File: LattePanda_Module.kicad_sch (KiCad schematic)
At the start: 3 parts

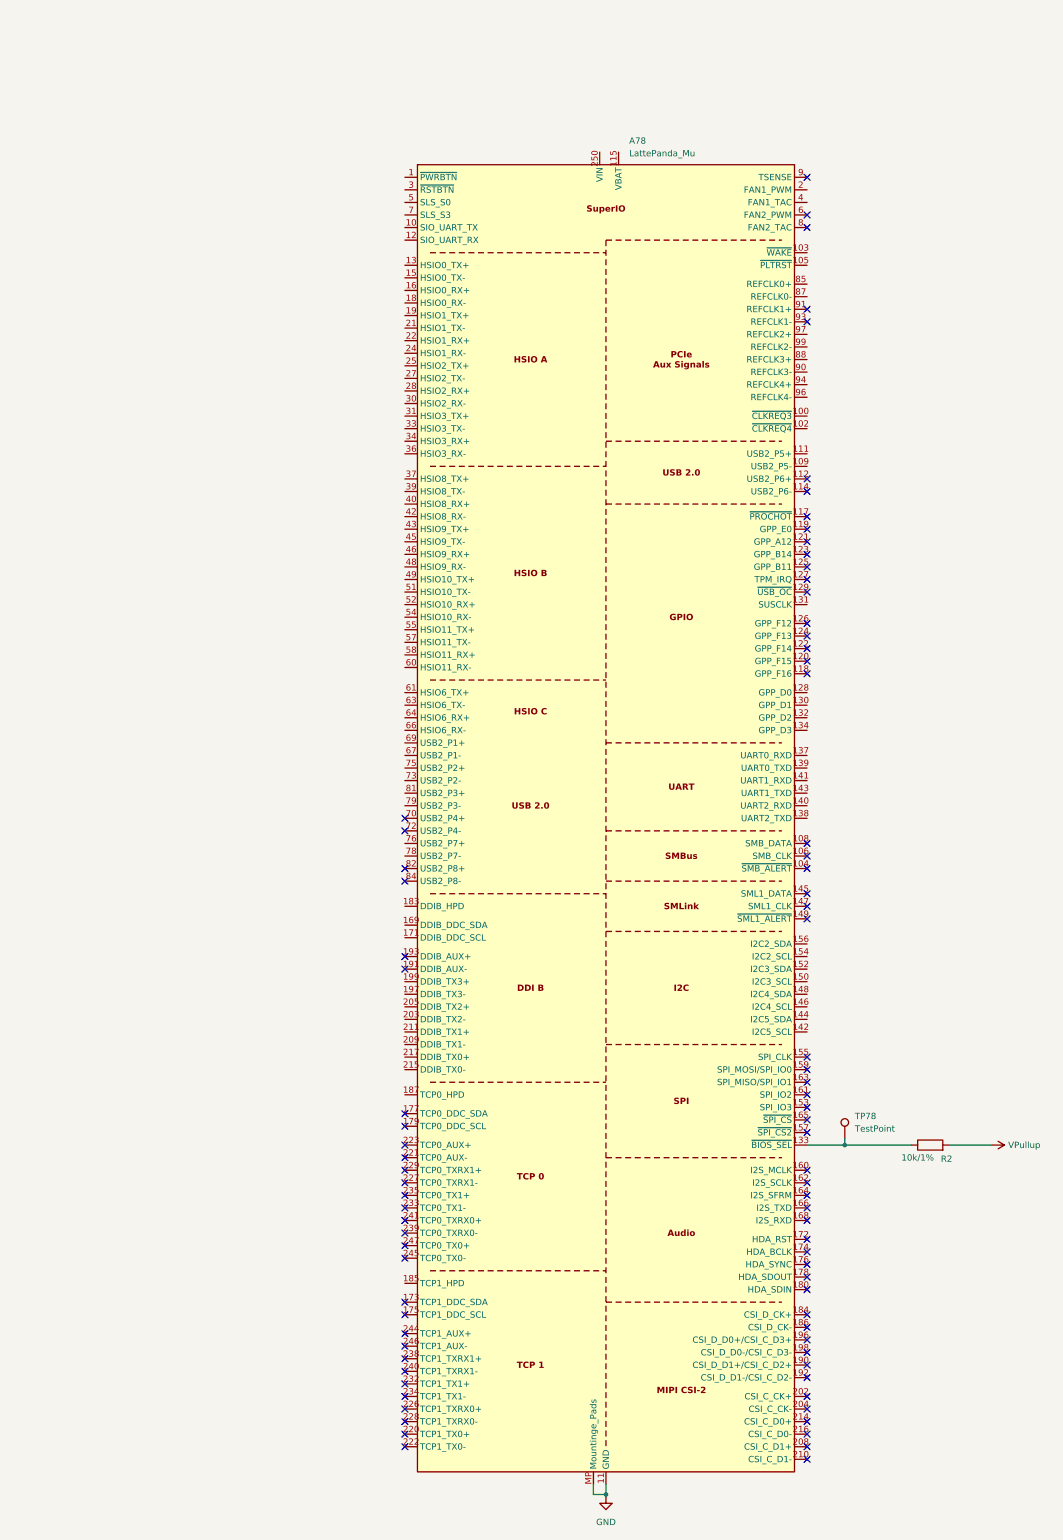
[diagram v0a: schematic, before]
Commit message: Added module pin symnbols and pull down resistors
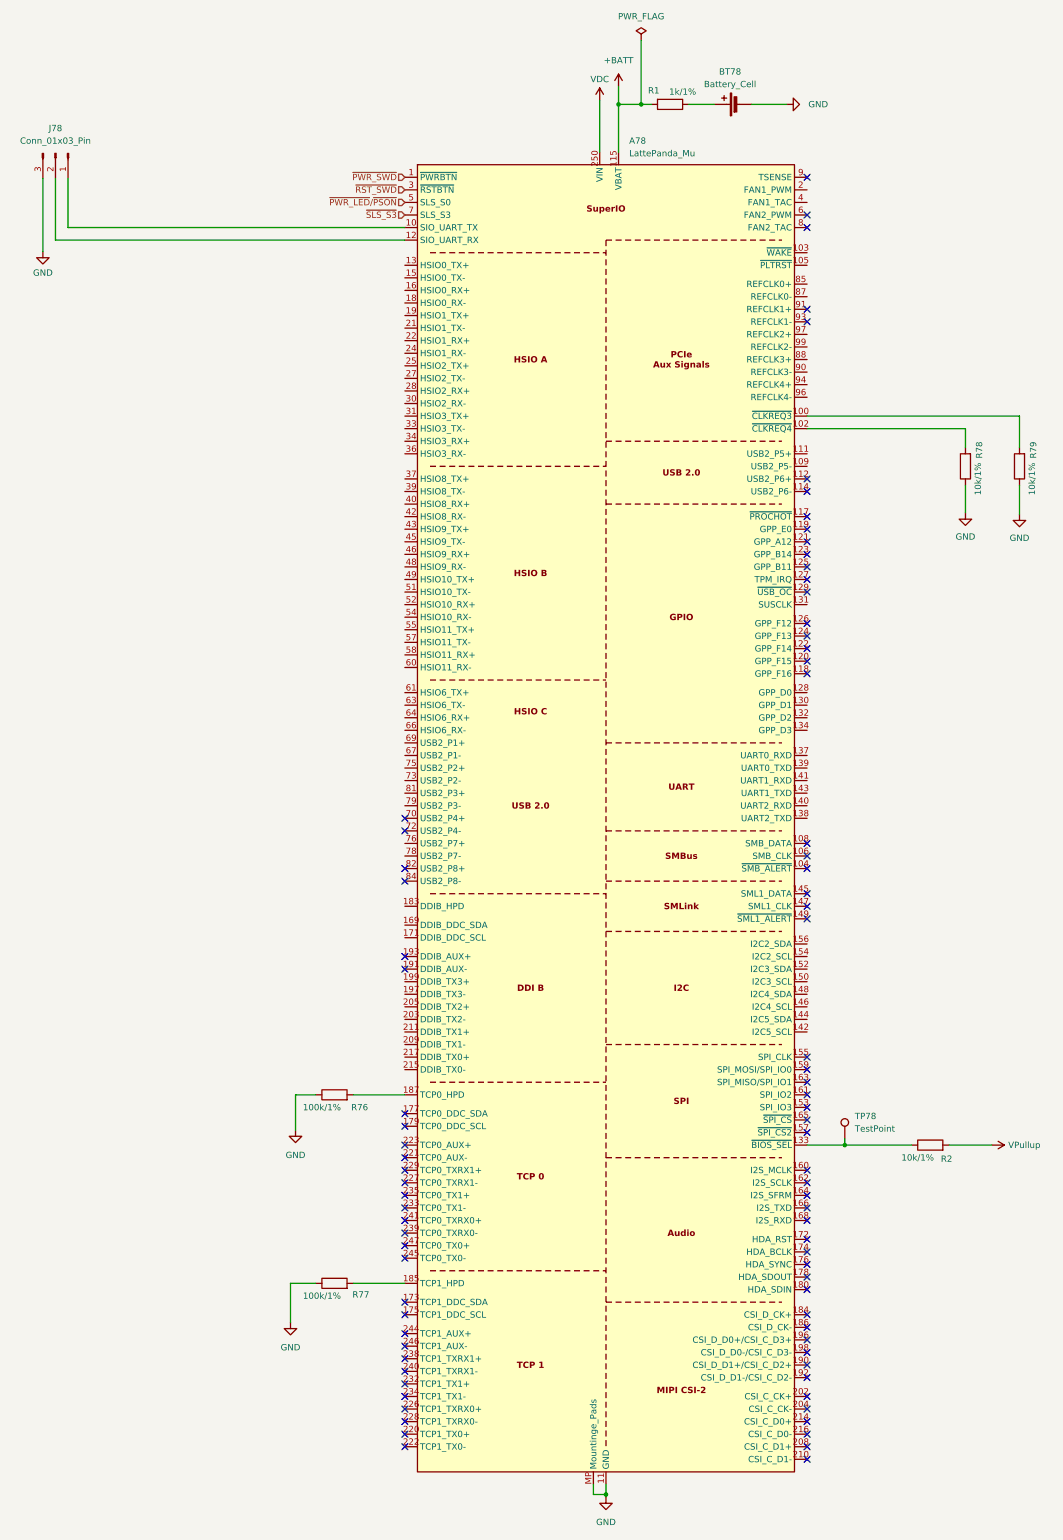
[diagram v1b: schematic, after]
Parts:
- added BT78: Battery_Cell, symbol Device:Battery_Cell
- added J78: Conn_01x03_Pin, A_HDJ_Library:PinHeader_1x03_P2.54mm_Vertical, symbol Connector:Conn_01x03_Pin
- added R1: 1k/1%, symbol Device:R
- added R76, R77: 100k/1%, symbol Device:R
- added R78, R79: 10k/1%, symbol Device:R
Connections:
- net GND: now also BT78.2 (-), J78.3 (Pin_3), R76.1, R77.1, R78.1, R79.1
- net ~{PWR_SWD}: now reaches A78.1 (~{PWRBTN})
- net at A78.10 (SIO_UART_TX): now also J78.1 (Pin_1)
- net at A78.100 (~{CLKREQ3}): now also R79.2
- net at A78.102 (~{CLKREQ4}): now also R78.2
- net +BATT: now reaches A78.115 (VBAT)
- net +BATT: now also R1.2
- net at A78.12 (SIO_UART_RX): now also J78.2 (Pin_2)
- net at A78.185 (TCP1_HPD): now also R77.2
- net at A78.187 (TCP0_HPD): now also R76.2
- net VDC: now reaches A78.250 (VIN), A78.251 (VIN), A78.252 (VIN), A78.253 (VIN), A78.254 (VIN), A78.255 (VIN), A78.256 (VIN), A78.257 (VIN), A78.258 (VIN), A78.259 (VIN), A78.260 (VIN)
- net ~{RST_SWD}: now reaches A78.3 (~{RSTBTN})
- net ~{PWR_LED}/~{PSON}: now reaches A78.5 (SLS_S0)
- net ~{SLS_S3}: now reaches A78.7 (SLS_S3)
- new net: BT78.1 (+), R1.1

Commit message: Hierichal labels added for the modul sheet
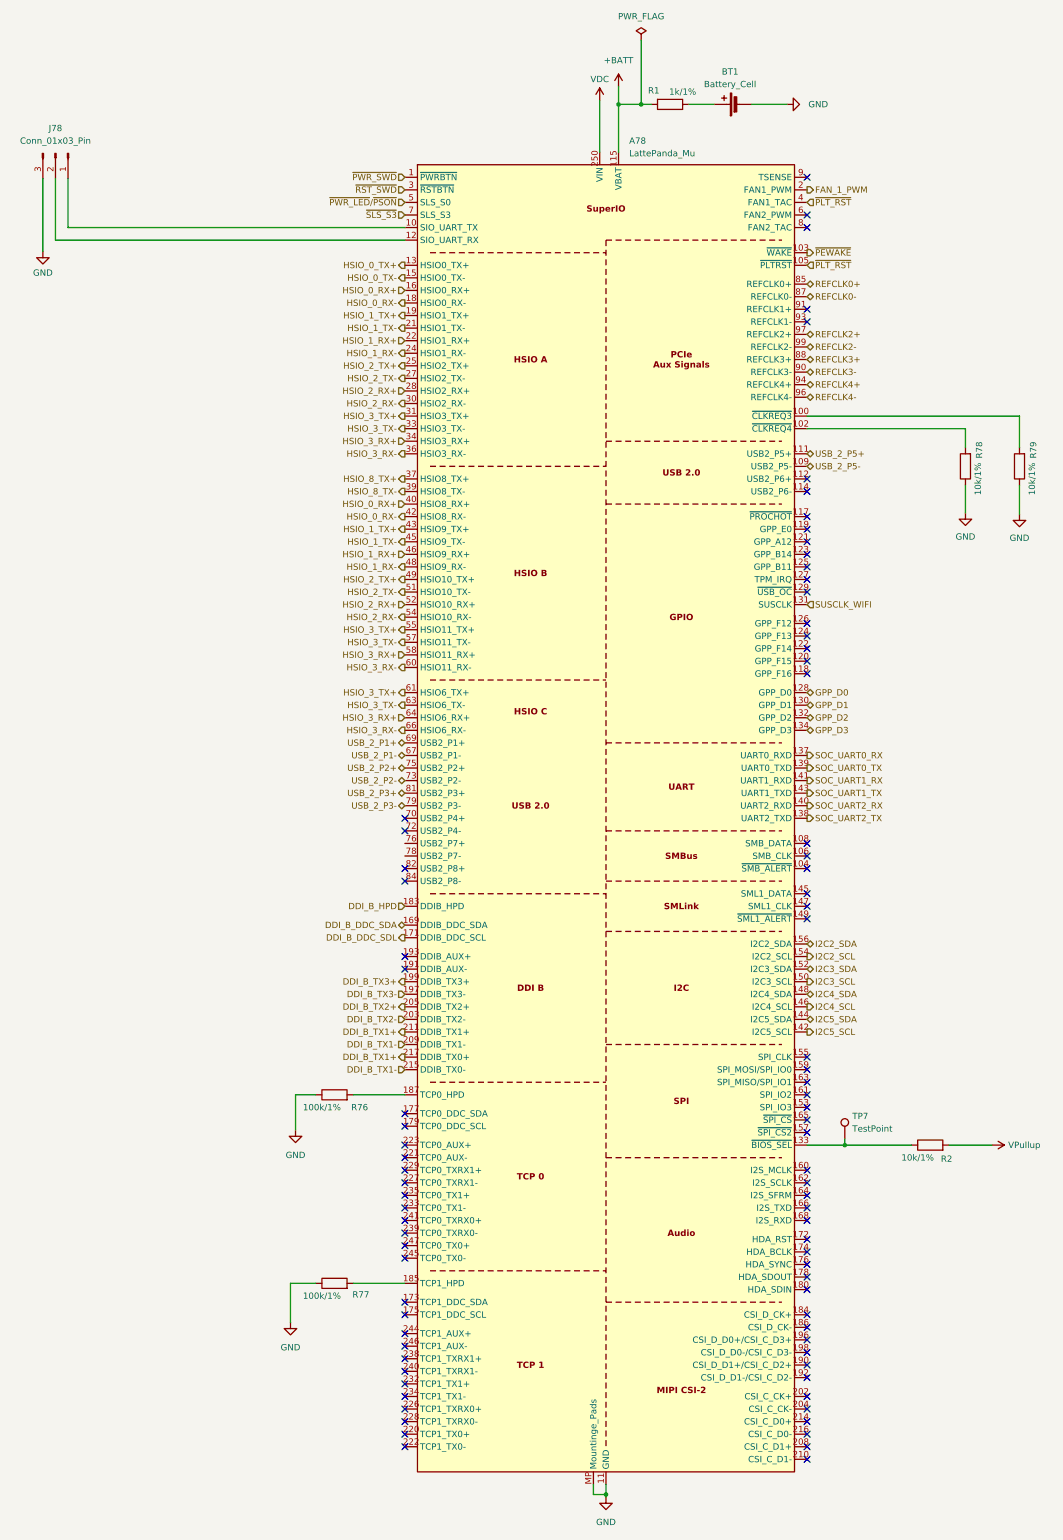
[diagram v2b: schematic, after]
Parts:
- renumbered BT78 to BT1, TP78 to TP7
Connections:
- net ~{PEWAKE}: now reaches A78.103 (~{WAKE})
- net ~{PLT_RST}: now reaches A78.105 (~{PLTRST})
- net ~{PLT_RST}: now also A78.4 (FAN1_TAC)
- net USB_2_P5-: now reaches A78.109 (USB2_P5-)
- net USB_2_P5+: now reaches A78.111 (USB2_P5+)
- net GPP_D0: now reaches A78.128 (GPP_D0)
- net HSIO_0_TX+: now reaches A78.13 (HSIO0_TX+)
- net GPP_D1: now reaches A78.130 (GPP_D1)
- net SUSCLK_WIFI: now reaches A78.131 (SUSCLK)
- net GPP_D2: now reaches A78.132 (GPP_D2)
- net GPP_D3: now reaches A78.134 (GPP_D3)
- net SOC_UART0_RX: now reaches A78.137 (UART0_RXD)
- net SOC_UART2_TX: now reaches A78.138 (UART2_TXD)
- net SOC_UART0_TX: now reaches A78.139 (UART0_TXD)
- net SOC_UART2_RX: now reaches A78.140 (UART2_RXD)
- net SOC_UART1_RX: now reaches A78.141 (UART1_RXD)
- net I2C5_SCL: now reaches A78.142 (I2C5_SCL)
- net SOC_UART1_TX: now reaches A78.143 (UART1_TXD)
- net I2C5_SDA: now reaches A78.144 (I2C5_SDA)
- net I2C4_SCL: now reaches A78.146 (I2C4_SCL)
- net I2C4_SDA: now reaches A78.148 (I2C4_SDA)
- net HSIO_0_TX-: now reaches A78.15 (HSIO0_TX-)
- net I2C3_SCL: now reaches A78.150 (I2C3_SCL)
- net I2C3_SDA: now reaches A78.152 (I2C3_SDA)
- net I2C2_SCL: now reaches A78.154 (I2C2_SCL)
- net I2C2_SDA: now reaches A78.156 (I2C2_SDA)
- net HSIO_0_RX+: now reaches A78.16 (HSIO0_RX+)
- net HSIO_0_RX+: now also A78.40 (HSIO8_RX+)
- net DDI_B_DDC_SDA: now reaches A78.169 (DDIB_DDC_SDA)
- net DDI_B_DDC_SDL: now reaches A78.171 (DDIB_DDC_SCL)
- net HSIO_0_RX-: now reaches A78.18 (HSIO0_RX-)
- net HSIO_0_RX-: now also A78.42 (HSIO8_RX-)
- net DDI_B_HPD: now reaches A78.183 (DDIB_HPD)
- net HSIO_1_TX+: now reaches A78.19 (HSIO1_TX+)
- net HSIO_1_TX+: now also A78.43 (HSIO9_TX+)
- net DDI_B_TX3-: now reaches A78.197 (DDIB_TX3-)
- net DDI_B_TX3+: now reaches A78.199 (DDIB_TX3+)
- net FAN_1_PWM: now reaches A78.2 (FAN1_PWM)
- net DDI_B_TX2-: now reaches A78.203 (DDIB_TX2-)
- net DDI_B_TX2+: now reaches A78.205 (DDIB_TX2+)
- net DDI_B_TX1-: now reaches A78.209 (DDIB_TX1-)
- net DDI_B_TX1-: now also A78.215 (DDIB_TX0-)
- net HSIO_1_TX-: now reaches A78.21 (HSIO1_TX-)
- net HSIO_1_TX-: now also A78.45 (HSIO9_TX-)
- net DDI_B_TX1+: now reaches A78.211 (DDIB_TX1+)
- net DDI_B_TX1+: now also A78.217 (DDIB_TX0+)
- net HSIO_1_RX+: now reaches A78.22 (HSIO1_RX+)
- net HSIO_1_RX+: now also A78.46 (HSIO9_RX+)
- net HSIO_1_RX-: now reaches A78.24 (HSIO1_RX-)
- net HSIO_1_RX-: now also A78.48 (HSIO9_RX-)
- net HSIO_2_TX+: now reaches A78.25 (HSIO2_TX+)
- net HSIO_2_TX+: now also A78.49 (HSIO10_TX+)
- net HSIO_2_TX-: now reaches A78.27 (HSIO2_TX-)
- net HSIO_2_TX-: now also A78.51 (HSIO10_TX-)
- net HSIO_2_RX+: now reaches A78.28 (HSIO2_RX+)
- net HSIO_2_RX+: now also A78.52 (HSIO10_RX+)
- net HSIO_2_RX-: now reaches A78.30 (HSIO2_RX-)
- net HSIO_2_RX-: now also A78.54 (HSIO10_RX-)
- net HSIO_3_TX+: now reaches A78.31 (HSIO3_TX+)
- net HSIO_3_TX+: now also A78.55 (HSIO11_TX+), A78.61 (HSIO6_TX+)
- net HSIO_3_TX-: now reaches A78.33 (HSIO3_TX-)
- net HSIO_3_TX-: now also A78.57 (HSIO11_TX-), A78.63 (HSIO6_TX-)
- net HSIO_3_RX+: now reaches A78.34 (HSIO3_RX+)
- net HSIO_3_RX+: now also A78.58 (HSIO11_RX+), A78.64 (HSIO6_RX+)
- net HSIO_3_RX-: now reaches A78.36 (HSIO3_RX-)
- net HSIO_3_RX-: now also A78.60 (HSIO11_RX-), A78.66 (HSIO6_RX-)
- net HSIO_8_TX+: now reaches A78.37 (HSIO8_TX+)
- net HSIO_8_TX-: now reaches A78.39 (HSIO8_TX-)
- net USB_2_P1-: now reaches A78.67 (USB2_P1-)
- net USB_2_P1+: now reaches A78.69 (USB2_P1+)
- net USB_2_P2-: now reaches A78.73 (USB2_P2-)
- net USB_2_P2+: now reaches A78.75 (USB2_P2+)
- net USB_2_P3-: now reaches A78.79 (USB2_P3-)
- net USB_2_P3+: now reaches A78.81 (USB2_P3+)
- net REFCLK0+: now reaches A78.85 (REFCLK0+)
- net REFCLK0-: now reaches A78.87 (REFCLK0-)
- net REFCLK3+: now reaches A78.88 (REFCLK3+)
- net REFCLK3-: now reaches A78.90 (REFCLK3-)
- net REFCLK4+: now reaches A78.94 (REFCLK4+)
- net REFCLK4-: now reaches A78.96 (REFCLK4-)
- net REFCLK2+: now reaches A78.97 (REFCLK2+)
- net REFCLK2-: now reaches A78.99 (REFCLK2-)

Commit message: Rearranged the hiearchal labels in module and main sheets
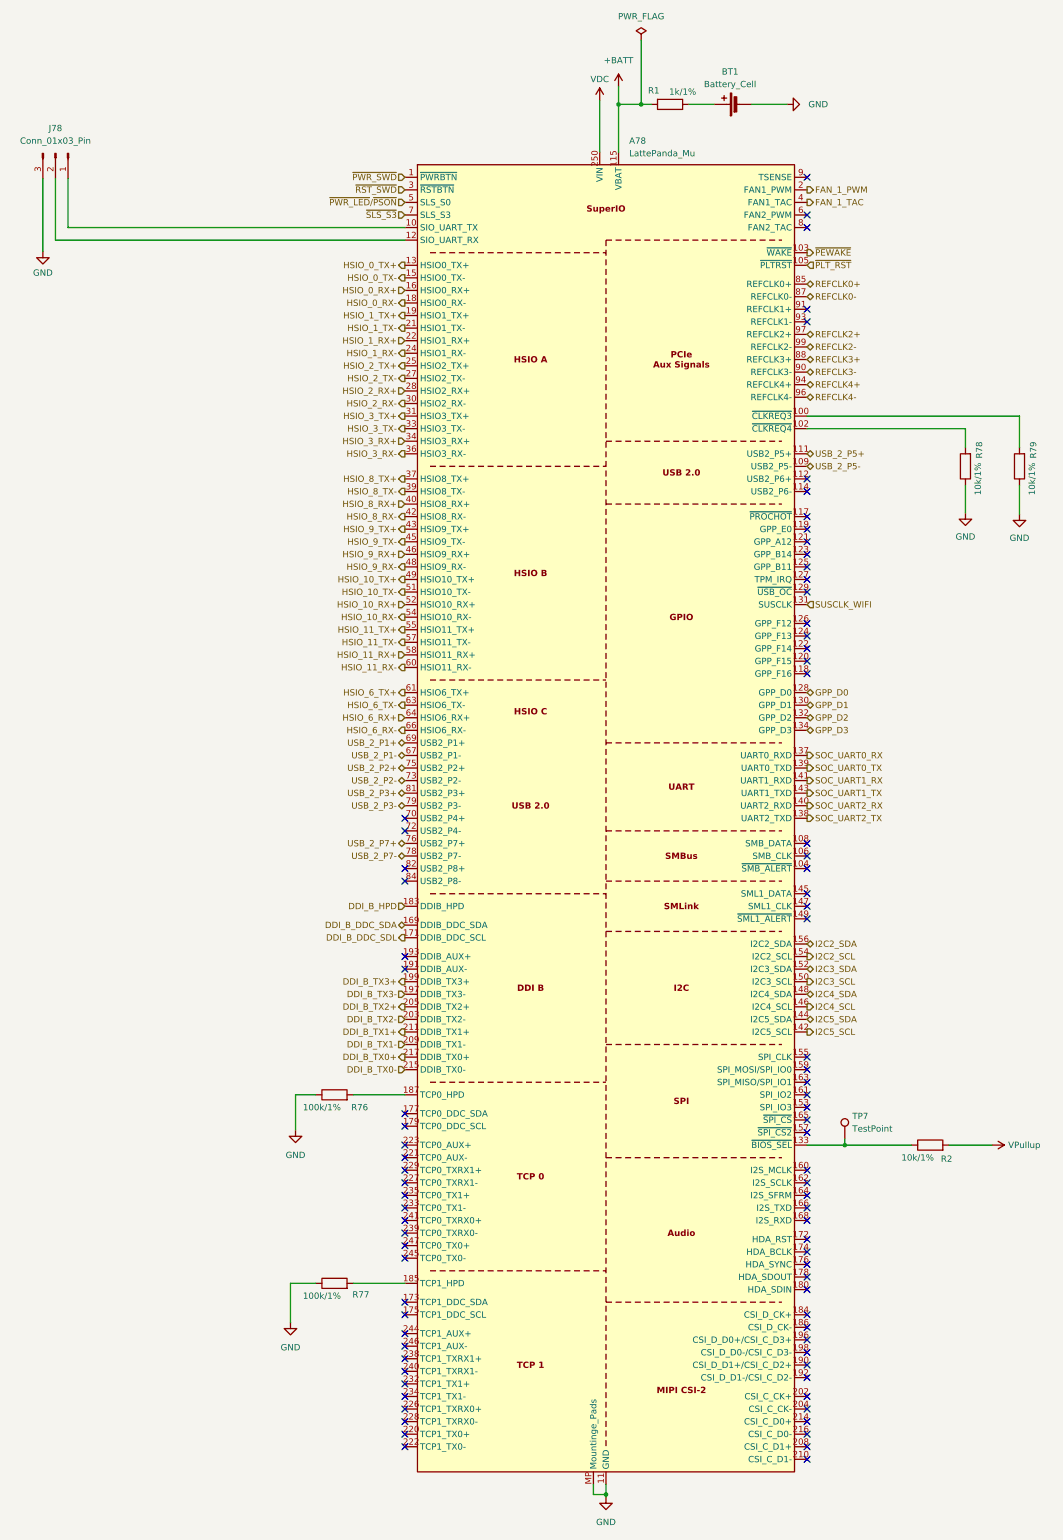
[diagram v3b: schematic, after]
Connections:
- net DDI_B_TX1+: no longer A78.217 (DDIB_TX0+)
- net DDI_B_TX1-: no longer A78.215 (DDIB_TX0-)
- net HSIO_0_RX+: no longer A78.40 (HSIO8_RX+)
- net HSIO_0_RX-: no longer A78.42 (HSIO8_RX-)
- net HSIO_1_RX+: no longer A78.46 (HSIO9_RX+)
- net HSIO_1_RX-: no longer A78.48 (HSIO9_RX-)
- net HSIO_1_TX+: no longer A78.43 (HSIO9_TX+)
- net HSIO_1_TX-: no longer A78.45 (HSIO9_TX-)
- net HSIO_2_RX+: no longer A78.52 (HSIO10_RX+)
- net HSIO_2_RX-: no longer A78.54 (HSIO10_RX-)
- net HSIO_2_TX+: no longer A78.49 (HSIO10_TX+)
- net HSIO_2_TX-: no longer A78.51 (HSIO10_TX-)
- net HSIO_3_RX+: no longer A78.58 (HSIO11_RX+), A78.64 (HSIO6_RX+)
- net HSIO_3_RX-: no longer A78.60 (HSIO11_RX-), A78.66 (HSIO6_RX-)
- net HSIO_3_TX+: no longer A78.55 (HSIO11_TX+), A78.61 (HSIO6_TX+)
- net HSIO_3_TX-: no longer A78.57 (HSIO11_TX-), A78.63 (HSIO6_TX-)
- net ~{PLT_RST}: no longer A78.4 (FAN1_TAC)
- net USB_2_P7+: now reaches A78.76 (USB2_P7+)
- net USB_2_P7-: now reaches A78.78 (USB2_P7-)
- new net DDI_B_TX0+: A78.217 (DDIB_TX0+)
- new net DDI_B_TX0-: A78.215 (DDIB_TX0-)
- new net FAN_1_TAC: A78.4 (FAN1_TAC)
- new net HSIO_10_RX+: A78.52 (HSIO10_RX+)
- new net HSIO_10_RX-: A78.54 (HSIO10_RX-)
- new net HSIO_10_TX+: A78.49 (HSIO10_TX+)
- new net HSIO_10_TX-: A78.51 (HSIO10_TX-)
- new net HSIO_11_RX+: A78.58 (HSIO11_RX+)
- new net HSIO_11_RX-: A78.60 (HSIO11_RX-)
- new net HSIO_11_TX+: A78.55 (HSIO11_TX+)
- new net HSIO_11_TX-: A78.57 (HSIO11_TX-)
- new net HSIO_6_RX+: A78.64 (HSIO6_RX+)
- new net HSIO_6_RX-: A78.66 (HSIO6_RX-)
- new net HSIO_6_TX+: A78.61 (HSIO6_TX+)
- new net HSIO_6_TX-: A78.63 (HSIO6_TX-)
- new net HSIO_8_RX+: A78.40 (HSIO8_RX+)
- new net HSIO_8_RX-: A78.42 (HSIO8_RX-)
- new net HSIO_9_RX+: A78.46 (HSIO9_RX+)
- new net HSIO_9_RX-: A78.48 (HSIO9_RX-)
- new net HSIO_9_TX+: A78.43 (HSIO9_TX+)
- new net HSIO_9_TX-: A78.45 (HSIO9_TX-)

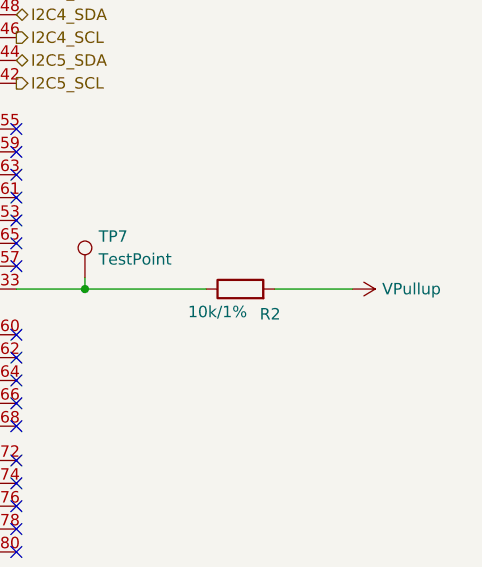
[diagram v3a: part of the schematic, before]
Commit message: Added the power and the restet button sub circuits to the psu shematic sheet
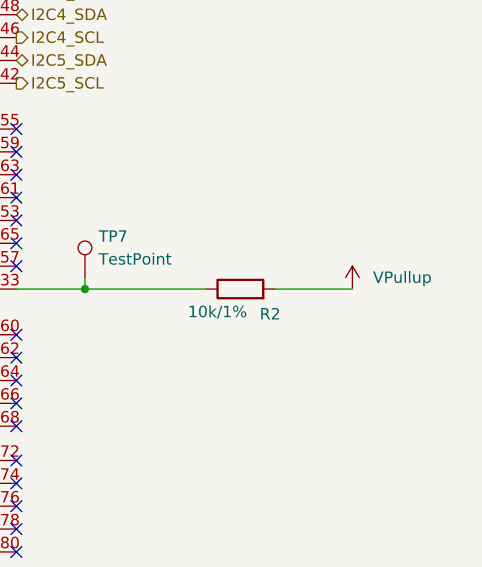
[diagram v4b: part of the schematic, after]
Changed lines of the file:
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@@
 	(symbol
 		(lib_id "power:+3V3")
-		(at 369.824 266.446 270)
+		(at 369.824 266.446 0)
 		(unit 1)
 		(body_style 1)
@@
 		(fields_autoplaced yes)
 		(property "Reference" "#PWR083"
-			(at 366.014 266.446 0)
+			(at 369.824 270.256 0)
 			(hide yes)
 			(show_name no)
@@
 		)
 		(property "Value" "VPullup"
-			(at 373.126 266.4459 90)
+			(at 372.11 265.1759 0)
 			(show_name no)
 			(do_not_autoplace no)
